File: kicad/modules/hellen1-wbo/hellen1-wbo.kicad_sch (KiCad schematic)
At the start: 65 parts, among them J600 Conn_02x03_Odd_Even, M600 Module-wbo-0.4, Q600 BTS3028, Q601 VNP28N04-E, U600 MCP6004, U601 AD8628, U602 STM32F042K6Tx, U603 REF3033, U604 XC6206P332MR, U605 TJA1051T/3/1J

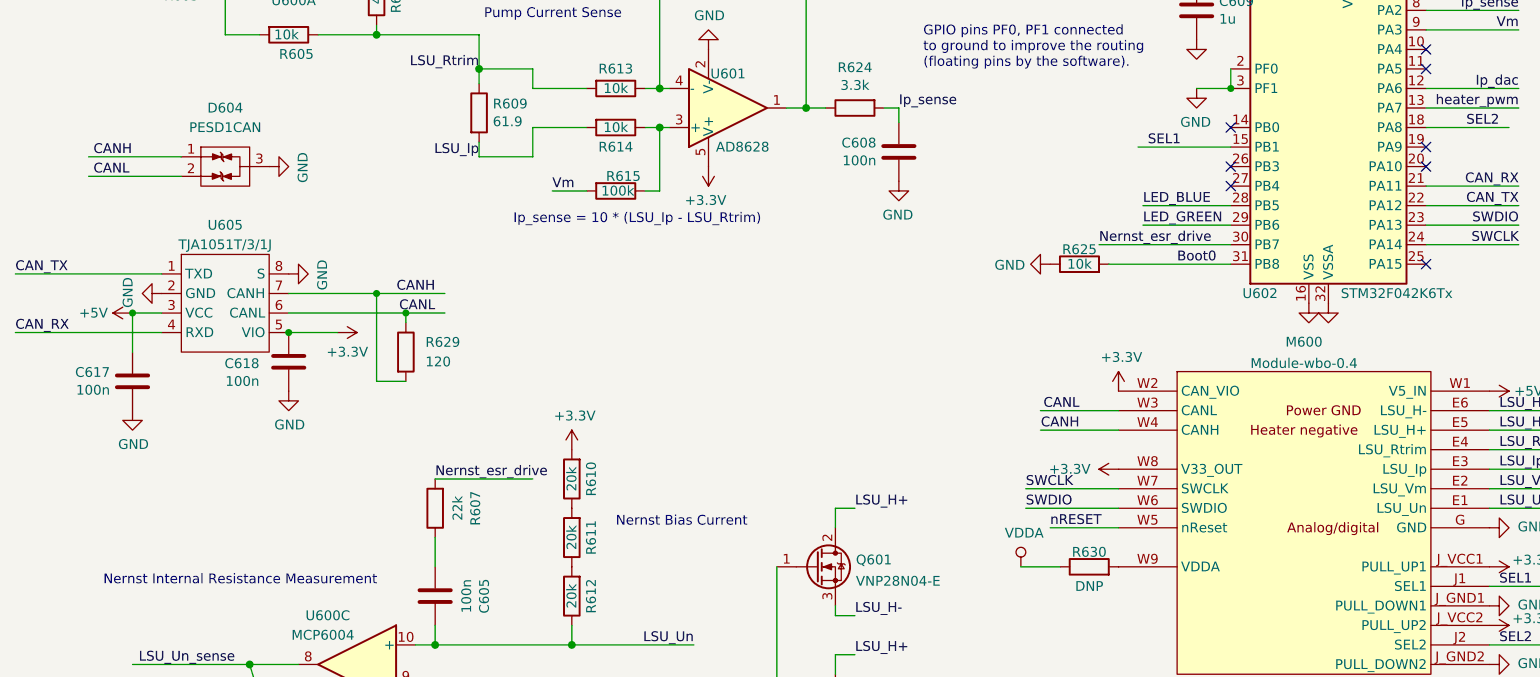
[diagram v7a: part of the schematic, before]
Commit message: Revert " #281 CANH and CANL aren`t flipped now"
This reverts commit b4a43784c1362e00eb4d70aed0e0eed805cb37d1.
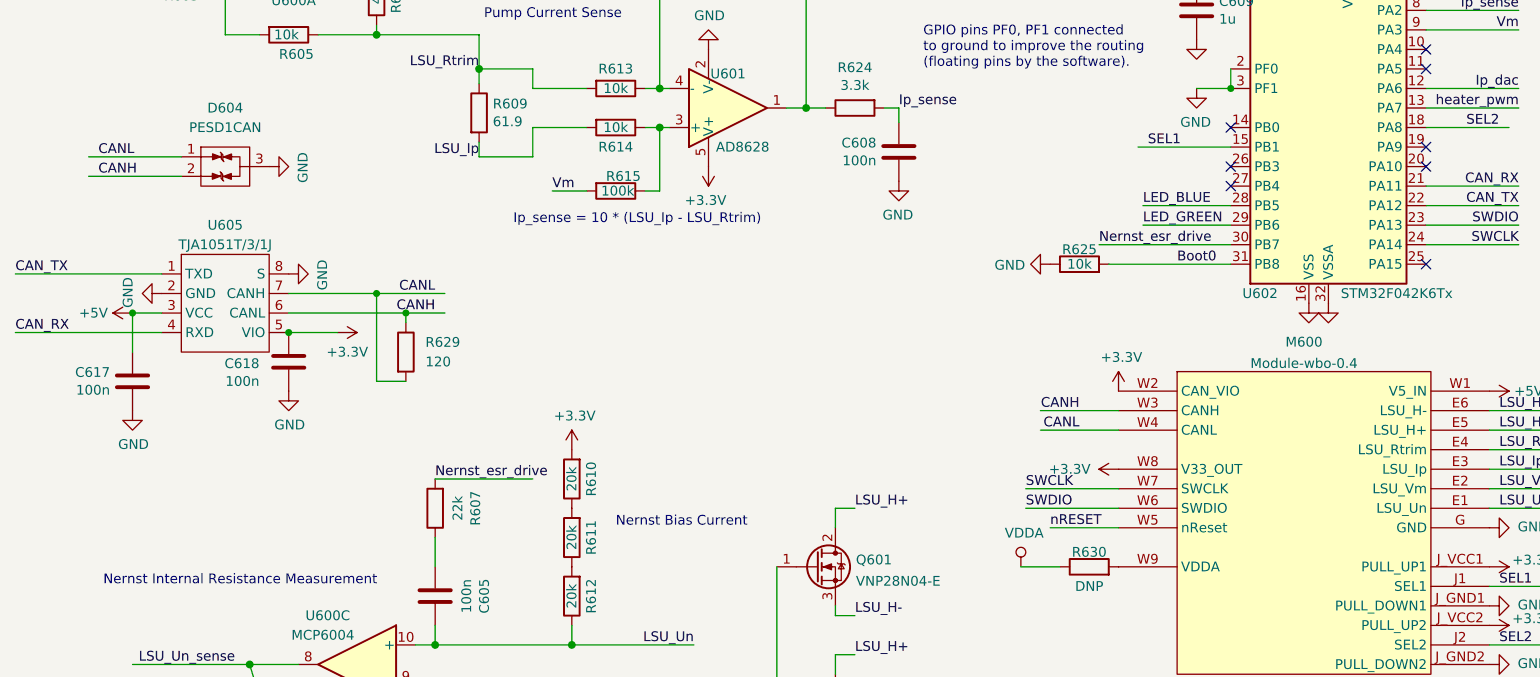
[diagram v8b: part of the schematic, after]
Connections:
- net CANH: now also D604.2 (D), M600.W3 (CANH), R629.1, U605.6 (CANL); no longer D604.1 (G), M600.W4 (CANH), R629.2, U605.7 (CANH)
- net CANL: now also D604.1 (G), M600.W4 (CANL), R629.2, U605.7 (CANH); no longer D604.2 (D), M600.W3 (CANL), R629.1, U605.6 (CANL)
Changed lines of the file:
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@@
     (effects (font (size 1.27 1.27)) (justify left bottom))
   )
-  (label "CANH" (at 72.39 111.76 180)
+  (label "CANH" (at 72.39 114.3 180)
     (effects (font (size 1.27 1.27)) (justify right bottom))
   )
@@
     (effects (font (size 1.27 1.27)) (justify right bottom))
   )
-  (label "CANH" (at 27.94 93.98 0)
+  (label "CANH" (at 28.575 96.52 0)
     (effects (font (size 1.27 1.27)) (justify left bottom))
   )
@@
     (effects (font (size 1.27 1.27)) (justify left bottom))
   )
-  (label "CANL" (at 27.94 96.52 0)
+  (label "CANL" (at 28.575 93.98 0)
     (effects (font (size 1.27 1.27)) (justify left bottom))
   )
@@
     (effects (font (size 1.27 1.27)) (justify right bottom))
   )
-  (label "CANH" (at 156.21 129.54 180)
+  (label "CANH" (at 156.21 127 180)
     (effects (font (size 1.27 1.27)) (justify right bottom))
   )
-  (label "CANL" (at 72.39 114.3 180)
+  (label "CANL" (at 72.39 111.76 180)
     (effects (font (size 1.27 1.27)) (justify right bottom))
   )
@@
     (effects (font (size 1.27 1.27)) (justify left bottom))
   )
-  (label "CANL" (at 156.21 127 180)
+  (label "CANL" (at 156.21 129.54 180)
     (effects (font (size 1.27 1.27)) (justify right bottom))
   )
